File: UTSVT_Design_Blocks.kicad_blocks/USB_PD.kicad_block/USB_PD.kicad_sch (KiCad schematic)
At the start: 28 parts, among them J1 USB4105-GF-A, Q1 Q_Dual_PMOS_G1S2G2D2S1D1, Q2 Q_Dual_PMOS_G1S2G2D2S1D1, U1 CYPD3177-24LQ

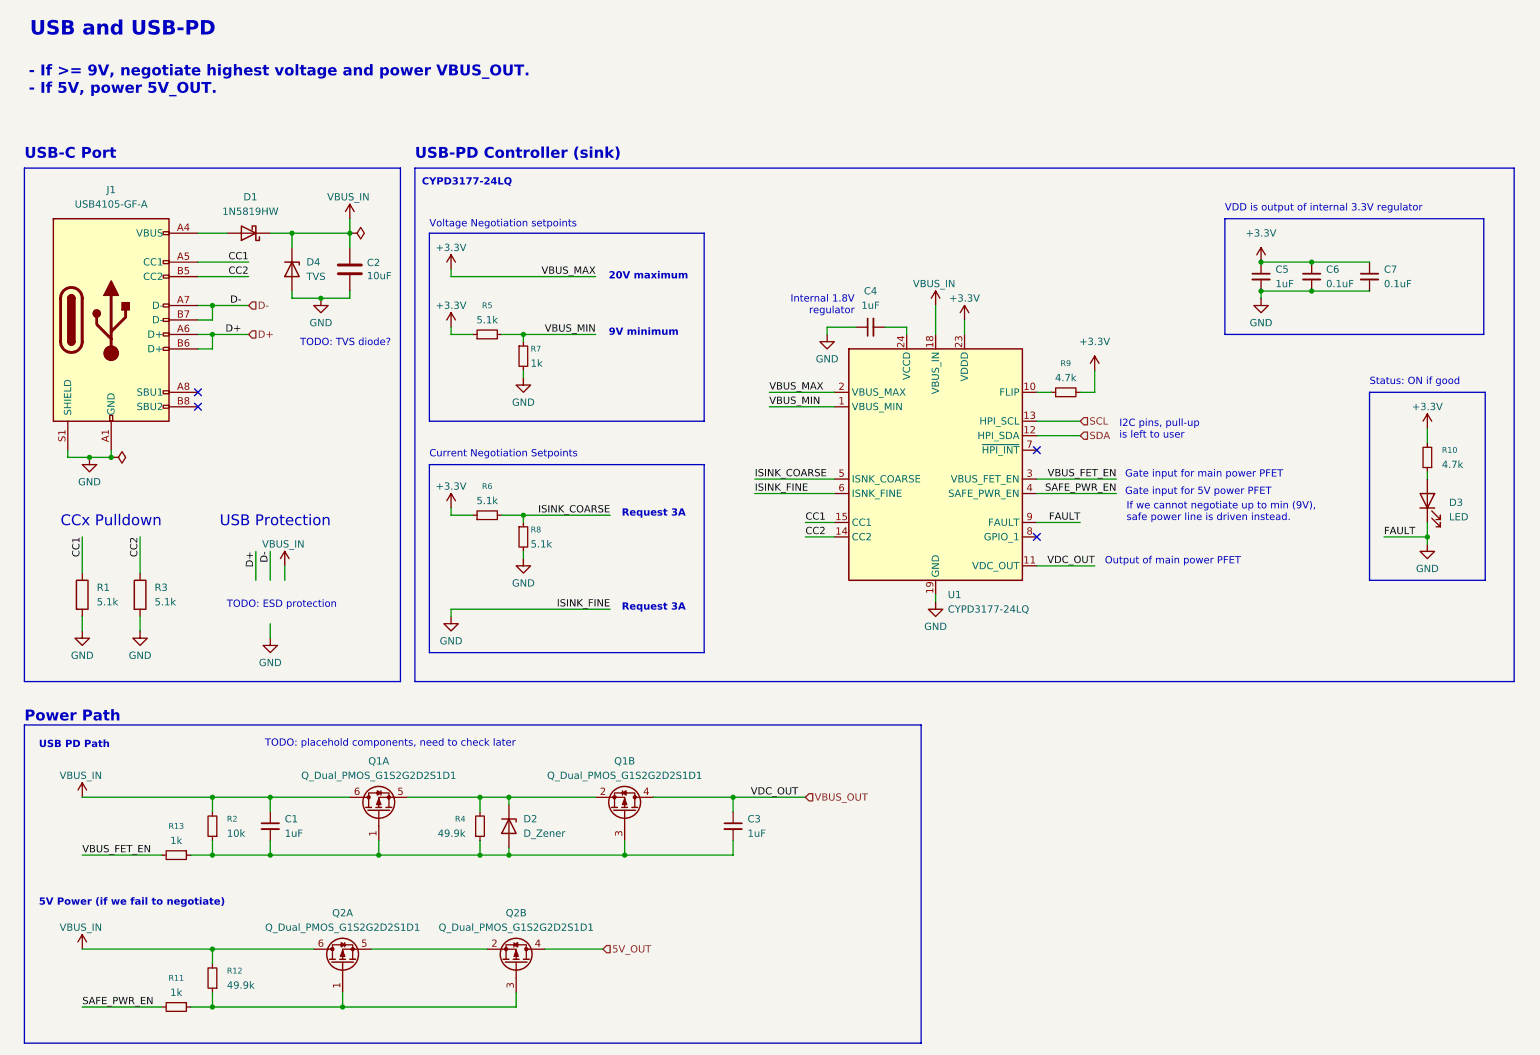
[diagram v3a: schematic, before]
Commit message: picked FETs, added TVS diodes for power path, USB, D+ D-
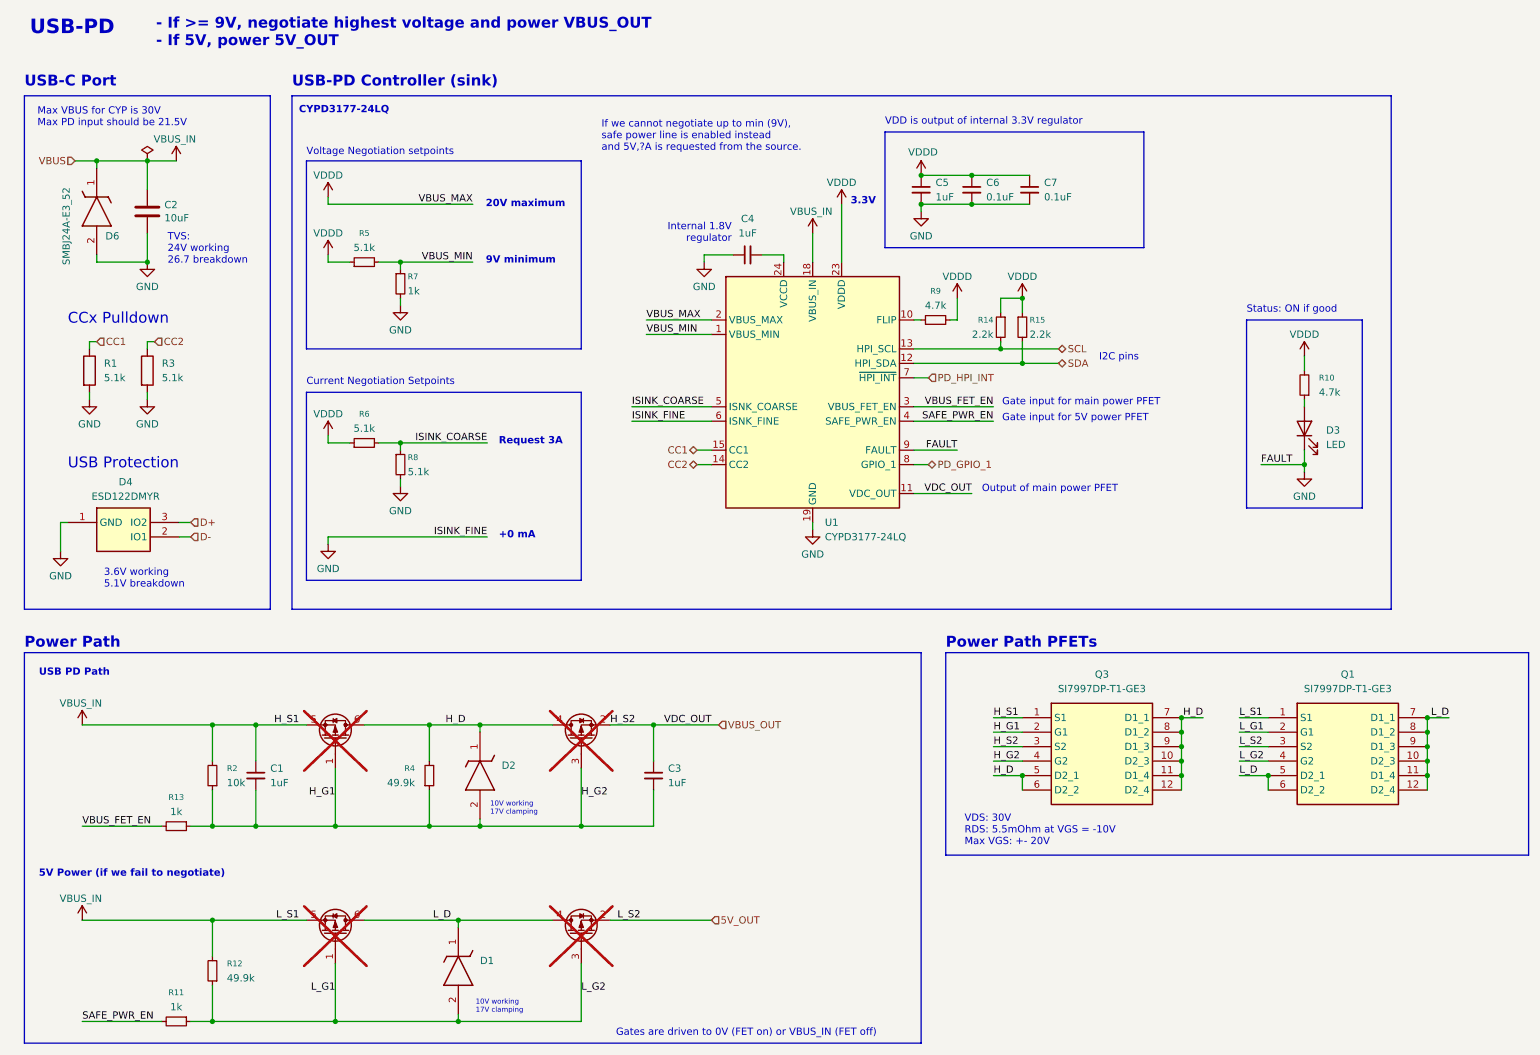
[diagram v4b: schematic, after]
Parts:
- removed D1: 1N5819HW, Diode_SMD:D_SOD-123, symbol Device:D_Schottky
- removed D2: D_Zener, symbol Device:D_Zener
- removed D4: TVS, symbol Device:D_Zener
- removed J1: USB4105-GF-A, UTSVT_Connectors:USB_C_Receptacle_GCT_USB4105-xx-A_16P_TopMnt_Horizontal, symbol Connector:USB_C_Receptacle_USB2.0_16P
- removed Q1: Q_Dual_PMOS_G1S2G2D2S1D1, symbol Transistor_FET:Q_Dual_PMOS_G1S2G2D2S1D1
- added D1, D2: SMBJ10A-E3_52, DIOM5436X244N, symbol SMBJ10A:SMBJ10A-E3_52
- added D4: ESD122DMYR, ESD122DMYR, symbol ESD122:ESD122DMYR
- added D6: SMBJ24A-E3_52, DIOM5436X244N, symbol SMBJ24A:SMBJ24A-E3_52
- added Q1, Q3: SI7997DP-T1-GE3, SI7288DPT1GE3, symbol SI7997DP:SI7997DP-T1-GE3
- added Q4: Q_Dual_PMOS_G1S2G2D2S1D1, symbol Transistor_FET:Q_Dual_PMOS_G1S2G2D2S1D1
- added R14, R15: 2.2k, symbol Device:R_Small
- Q2: now not fitted; now left out of the parts list
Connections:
- net 5V_OUT: now also Q2.2 (S), Q1.3 (S2); no longer Q2.4 (D)
- net D+: now also D4.3 (IO2)
- net D-: now also D4.2 (IO1)
- net GND: now also D4.1 (GND), D6.2 (A)
- net SCL: now also R14.2
- net SDA: now also R15.2
- net VBUS_IN: now also Q2.5 (S), D6.1 (K), Q1.1 (S1), Q3.1 (S1), Q4.5 (S); no longer Q2.6 (D)
- net VBUS_OUT: now also Q3.3 (S2), Q4.2 (S)
- net H_G1: now reaches C1.2, C3.2, R13.1, R2.1, R4.1
- net H_G1: now also D2.2 (A), Q3.2 (G1), Q3.4 (G2), Q4.1 (G), Q4.3 (G)
- net PD_HPI_INT: now reaches U1.7 (~{HPI_INT})
- net PD_GPIO_1: now reaches U1.8 (GPIO_1)
- net L_G1: now reaches Q2.1 (G), Q2.3 (G), R11.1, R12.1
- net L_G1: now also D1.2 (A), Q1.2 (G1), Q1.4 (G2)
- net H_D: now reaches R4.2
- net H_D: now also D2.1 (K), Q3.10 (D2_3), Q3.11 (D1_4), Q3.12 (D2_4), Q3.5 (D2_1), Q3.6 (D2_2), Q3.7 (D1_1), Q3.8 (D1_2), Q3.9 (D1_3), Q4.4 (D), Q4.6 (D)
- net +3.3V renamed VDDD
- net VDDD: now also R14.1, R15.1
- new net L_D: D1.1 (K), Q1.10 (D2_3), Q1.11 (D1_4), Q1.12 (D2_4), Q1.5 (D2_1), Q1.6 (D2_2), Q1.7 (D1_1), Q1.8 (D1_2), Q1.9 (D1_3), Q2.4 (D), Q2.6 (D)
- no-connect marks 4 -> 0
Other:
- note added: "+0 mA"
- note added: "- If >= 9V, negotiate highest voltage and power VBUS_OUT - If 5V, power 5V_OUT"
- note added: "10V working 17V clamping"
- note added: "3.3V"
- note added: "3.6V working 5.1V breakdown"
- note added: "Gates are driven to 0V (FET on) or VBUS_IN (FET off)"
- note added: "I2C pins"
- note added: "If we cannot negotiate up to min (9V), safe power line is enabled instead and 5V,?A is requested from the source."
- note added: "Max VBUS for CYP is 30V Max PD input should be 21.5V"
- note added: "Power Path PFETs"
- note added: "TVS: 24V working 26.7 breakdown"
- note added: "USB-PD"
- note added: "VDS: 30V RDS: 5.5mOhm at VGS = -10V Max VGS: +- 20V"
- note removed: "- If >= 9V, negotiate highest voltage and power VBUS_OUT. - If 5V, power 5V_OUT."
- note removed: "I2C pins, pull-up is left to user"
- note removed: "If we cannot negotiate up to min (9V), safe power line is driven instead."
- note removed: "TODO: ESD protection"
- note removed: "TODO: TVS diode?"
- note removed: "TODO: placehold components, need to check later"
- note removed: "USB and USB-PD"
- moved on the sheet: C1, C2, C3, C4, C5, C6, C7, D3, R1, R10, R11, R12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

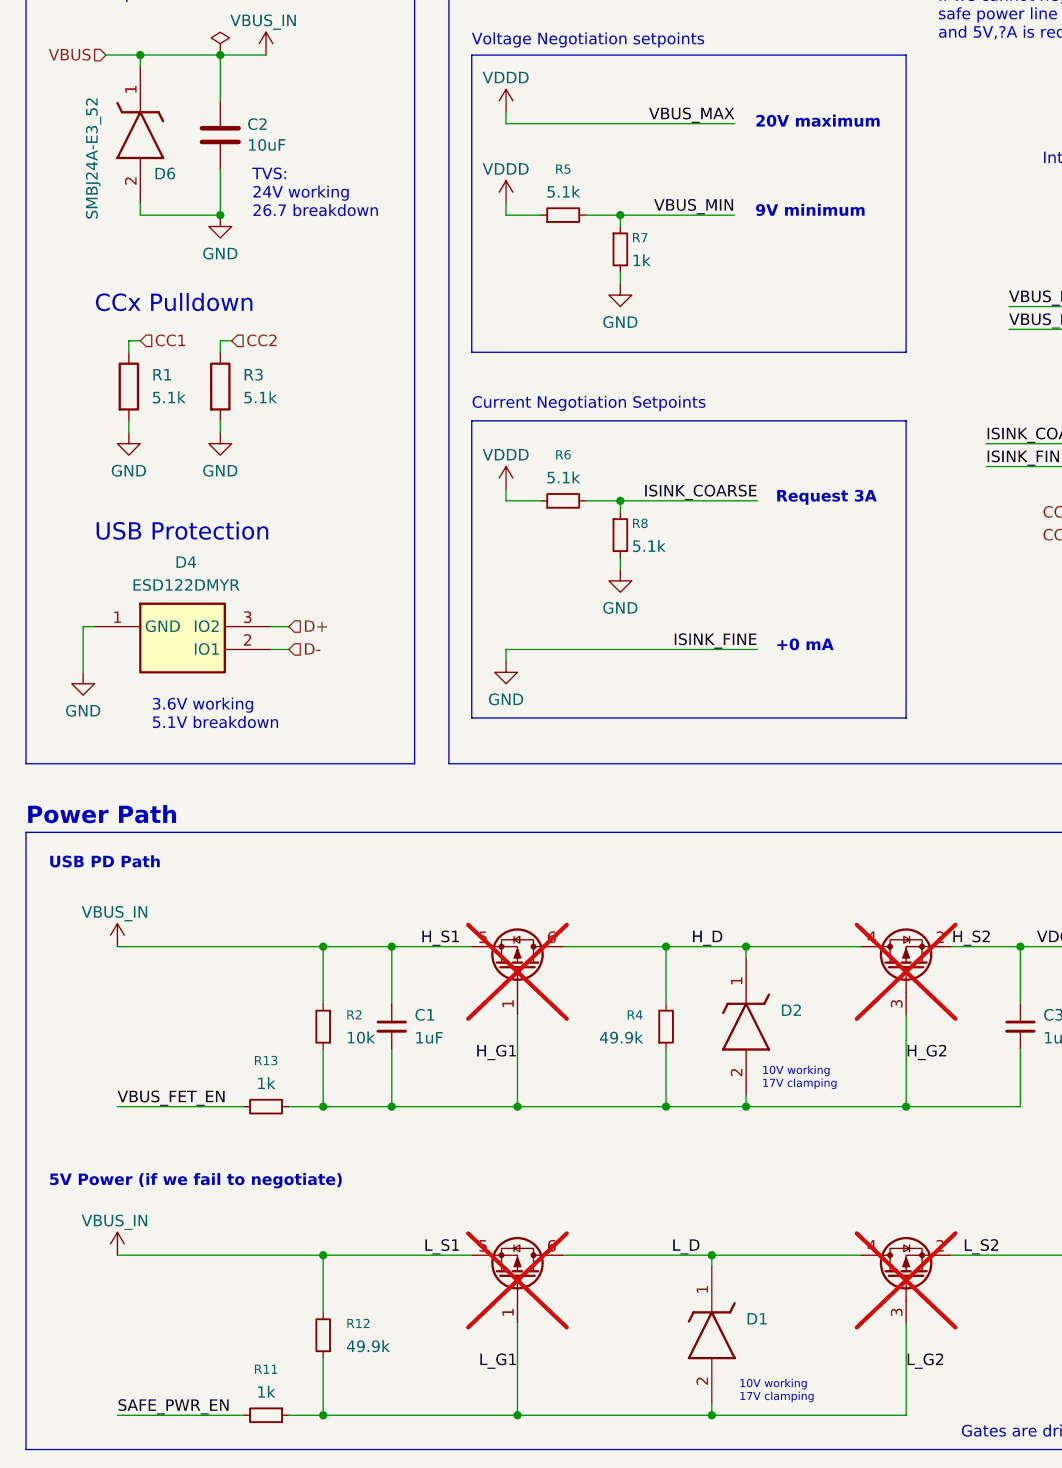
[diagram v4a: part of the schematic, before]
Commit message: changed D+ D- diode bc the old one was highk microscopic
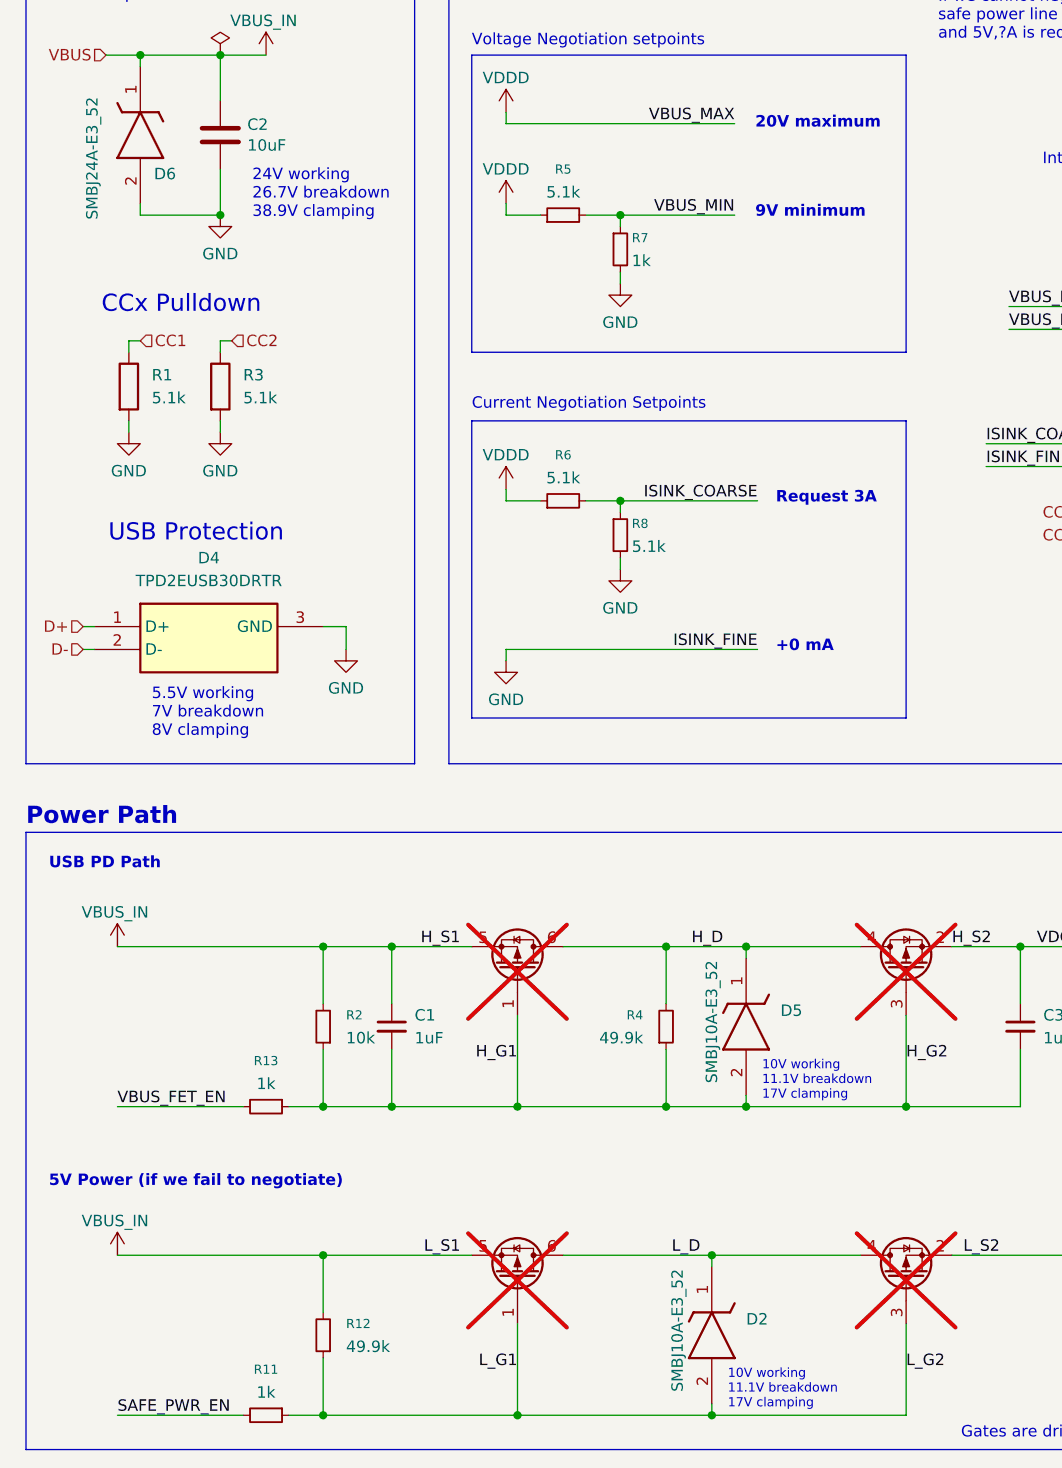
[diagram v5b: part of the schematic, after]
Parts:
- removed D1: SMBJ10A-E3_52, DIOM5436X244N, symbol SMBJ10A:SMBJ10A-E3_52
- removed D4: ESD122DMYR, ESD122DMYR, symbol ESD122:ESD122DMYR
- added D4: TPD2EUSB30DRTR, SOTFL35P100X50-3N, symbol TPD2EUSB30:TPD2EUSB30DRTR
- added D5: SMBJ10A-E3_52, DIOM5436X244N, symbol SMBJ10A:SMBJ10A-E3_52
- C1, C3, C4, C5, C6, C7: footprint (none) -> Capacitor_SMD:C_0603_1608Metric_Pad1.08x0.95mm_HandSolder
- D3: footprint (none) -> LED_SMD:LED_0603_1608Metric_Pad1.05x0.95mm_HandSolder
- D6: footprint DIOM5436X244N -> Components:DIOM5436X244N
- Q1, Q3: footprint SI7288DPT1GE3 -> Components:SI7288DPT1GE3
- R10, R11, R12, R13, R14, R15, R2, R4, R5, R6, R7, R8, R9: footprint (none) -> Resistor_SMD:R_0603_1608Metric_Pad0.98x0.95mm_HandSolder
- U1: footprint Package_DFN_QFN:QFN-24-1EP_4x4mm_P0.5mm_EP2.75x2.75mm -> Components:CYPD3177-24LQXQ
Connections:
- net D+: now also D4.1 (D+)
- net D-: now also D4.2 (D-)
- net GND: now also D4.3 (GND)
- net H_D: now also D5.1 (K); no longer D2.1 (K)
- net H_G1: now also D5.2 (A); no longer D2.2 (A)
- net L_D: now also D2.1 (K)
- net L_G1: now also D2.2 (A)
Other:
- note added: "10V working 11.1V breakdown 17V clamping"
- note added: "24V working 26.7V breakdown 38.9V clamping"
- note added: "5.5V working 7V breakdown 8V clamping"
- note removed: "10V working 17V clamping"
- note removed: "3.6V working 5.1V breakdown"
- note removed: "TVS: 24V working 26.7 breakdown"

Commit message: smth
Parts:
- D2, D5: footprint DIOM5436X244N -> Components:DIOM5436X244N
- D4: footprint SOTFL35P100X50-3N -> Components:TPD2EUSB30DRTR
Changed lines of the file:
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@@
 			)
 		)
-		(property "Footprint" "SOTFL35P100X50-3N"
+		(property "Footprint" "Components:TPD2EUSB30DRTR"
 			(at 44.45 199.06 0)
 			(effects
@@
 			)
 		)
-		(property "Footprint" "DIOM5436X244N"
+		(property "Footprint" "Components:DIOM5436X244N"
 			(at 1.6 151.13 0)
 			(effects
@@
 			)
 		)
-		(property "Footprint" "DIOM5436X244N"
+		(property "Footprint" "Components:DIOM5436X244N"
 			(at -2.21 185.42 0)
 			(effects

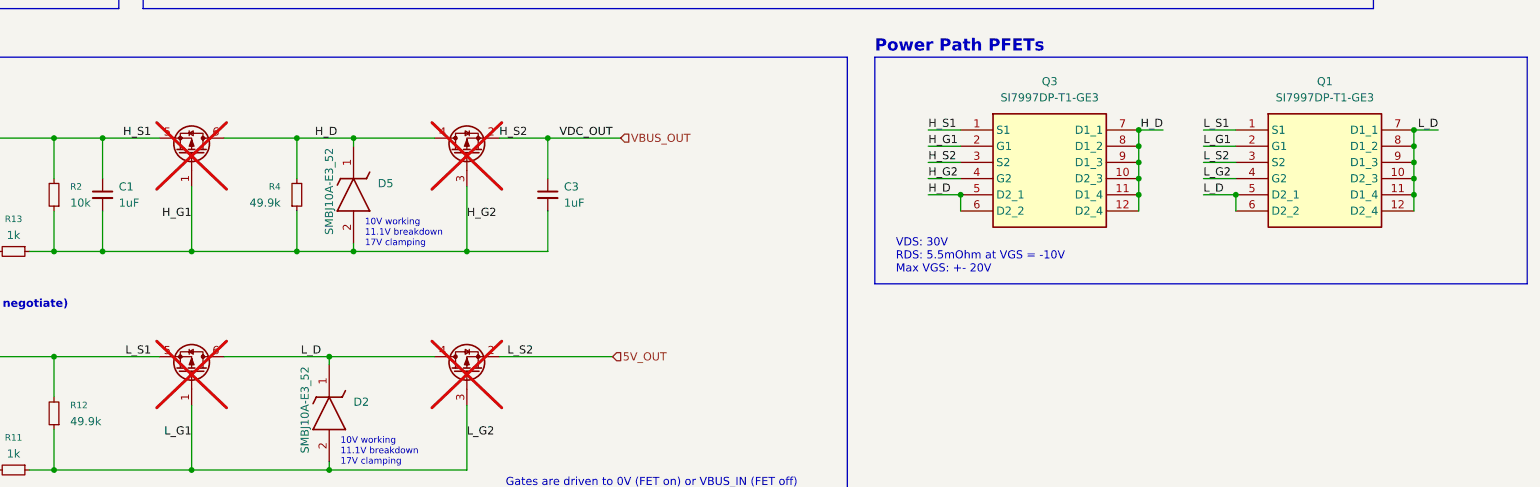
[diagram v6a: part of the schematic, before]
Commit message: flipped fets
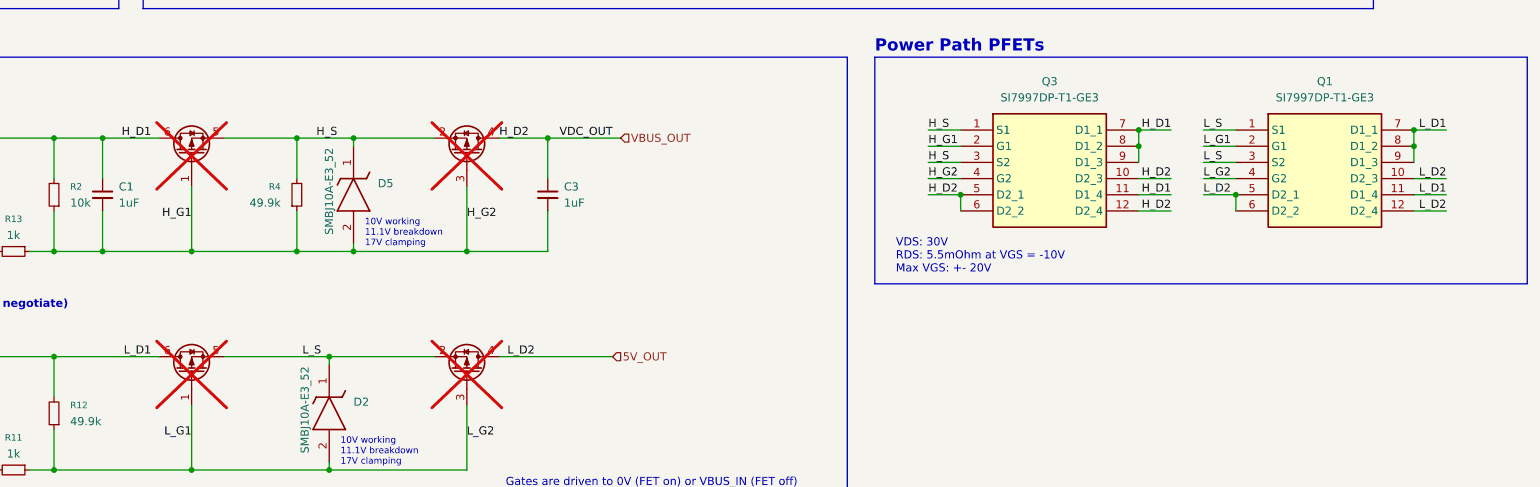
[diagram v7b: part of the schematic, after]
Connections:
- net 5V_OUT: now also Q1.10 (D2_3), Q1.12 (D2_4), Q1.5 (D2_1), Q1.6 (D2_2), Q2.4 (D); no longer Q1.3 (S2), Q2.2 (S)
- net VBUS_IN: now also Q1.11 (D1_4), Q1.7 (D1_1), Q1.8 (D1_2), Q1.9 (D1_3), Q2.6 (D), Q3.11 (D1_4), Q3.7 (D1_1), Q3.8 (D1_2), Q3.9 (D1_3), Q4.6 (D); no longer Q1.1 (S1), Q2.5 (S), Q3.1 (S1), Q4.5 (S)
- net VBUS_OUT: now also Q3.10 (D2_3), Q3.12 (D2_4), Q3.5 (D2_1), Q3.6 (D2_2), Q4.4 (D); no longer Q3.3 (S2), Q4.2 (S)
- removed net H_D: D5.1 (K), Q3.10 (D2_3), Q3.11 (D1_4), Q3.12 (D2_4), Q3.5 (D2_1), Q3.6 (D2_2), Q3.7 (D1_1), Q3.8 (D1_2), Q3.9 (D1_3), Q4.4 (D), Q4.6 (D), R4.2
- removed net L_D: D2.1 (K), Q1.10 (D2_3), Q1.11 (D1_4), Q1.12 (D2_4), Q1.5 (D2_1), Q1.6 (D2_2), Q1.7 (D1_1), Q1.8 (D1_2), Q1.9 (D1_3), Q2.4 (D), Q2.6 (D)
- new net H_S: D5.1 (K), Q3.1 (S1), Q3.3 (S2), Q4.2 (S), Q4.5 (S), R4.2
- new net L_S: D2.1 (K), Q1.1 (S1), Q1.3 (S2), Q2.2 (S), Q2.5 (S)
